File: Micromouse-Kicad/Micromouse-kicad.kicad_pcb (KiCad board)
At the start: 4 copper layers, 98.6 x 100 mm, 69 parts, among them J1 UARTBTH, J2 Batería, J3 VL6180x, J4 MotorEncodL, J5 MotorEncodR, Q1 BS170, Q2 BS170, Q3 BS170, Q4 BS170, SW1 PowerSwitch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

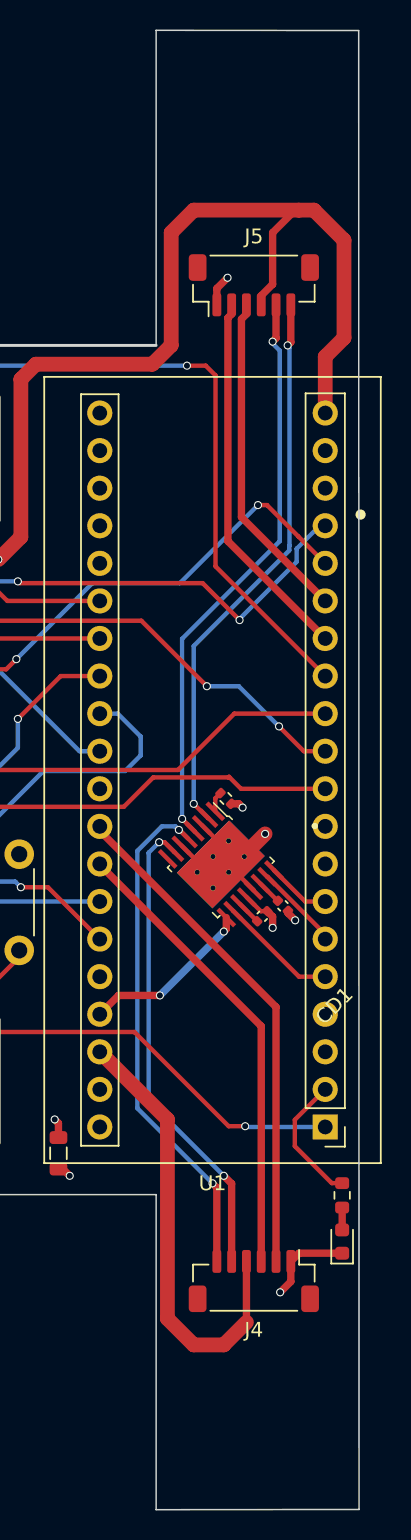
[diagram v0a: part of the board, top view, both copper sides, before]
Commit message: Modelos 3D completados
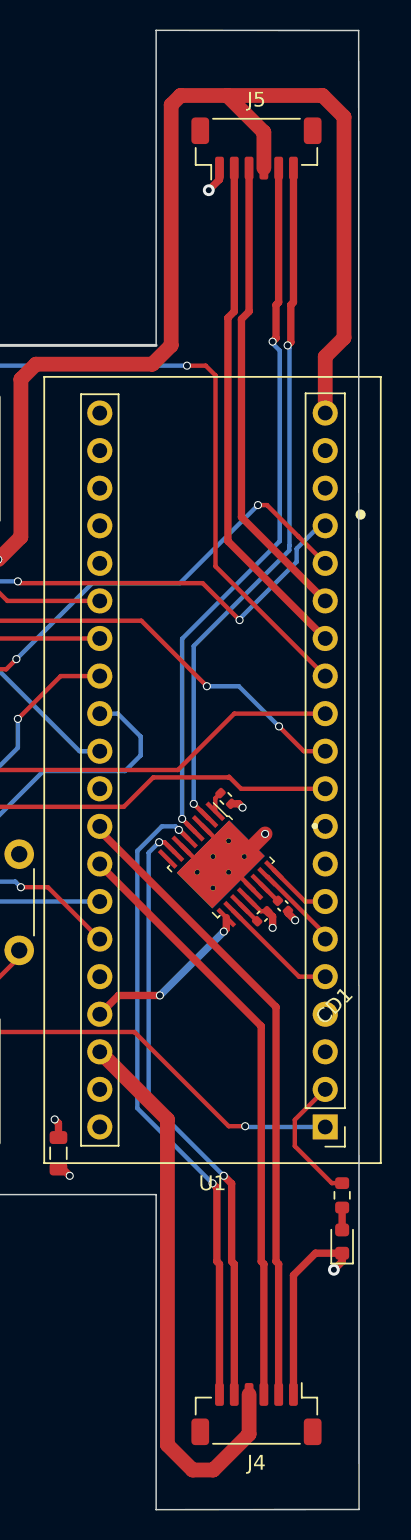
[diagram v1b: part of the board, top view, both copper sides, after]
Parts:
- moved J5 9.25 mm to (183.3, 60.6)
- moved J4 8.99 mm to (183.3, 146.2)
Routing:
- net +3.3V: track 144.7 -> 167.0 mm
- net TIM4_CH1: track 25.4 -> 34.7 mm
- net OutML2: track 39.0 -> 48.3 mm
- net OutML1: track 38.0 -> 47.3 mm
- net TIM4_CH2: track 22.5 -> 31.8 mm
- net TIM3_CH2: track 31.4 -> 40.5 mm
- net TIM3_CH1: track 34.3 -> 43.4 mm
- net OutMR2: track 34.4 -> 43.5 mm
- net OutMR1: track 32.3 -> 41.3 mm
- net GND: track 94.6 -> 101.5 mm

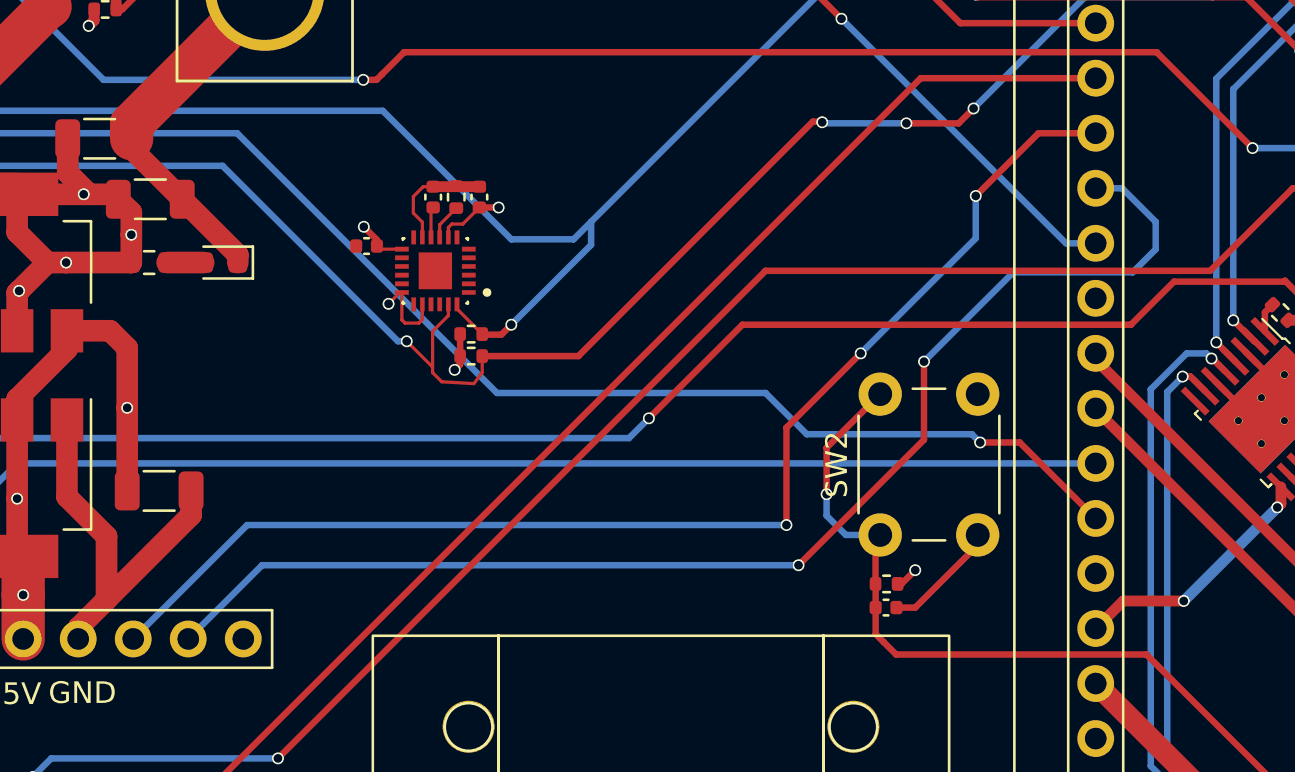
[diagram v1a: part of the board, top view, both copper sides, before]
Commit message: Arreglo bluetooth
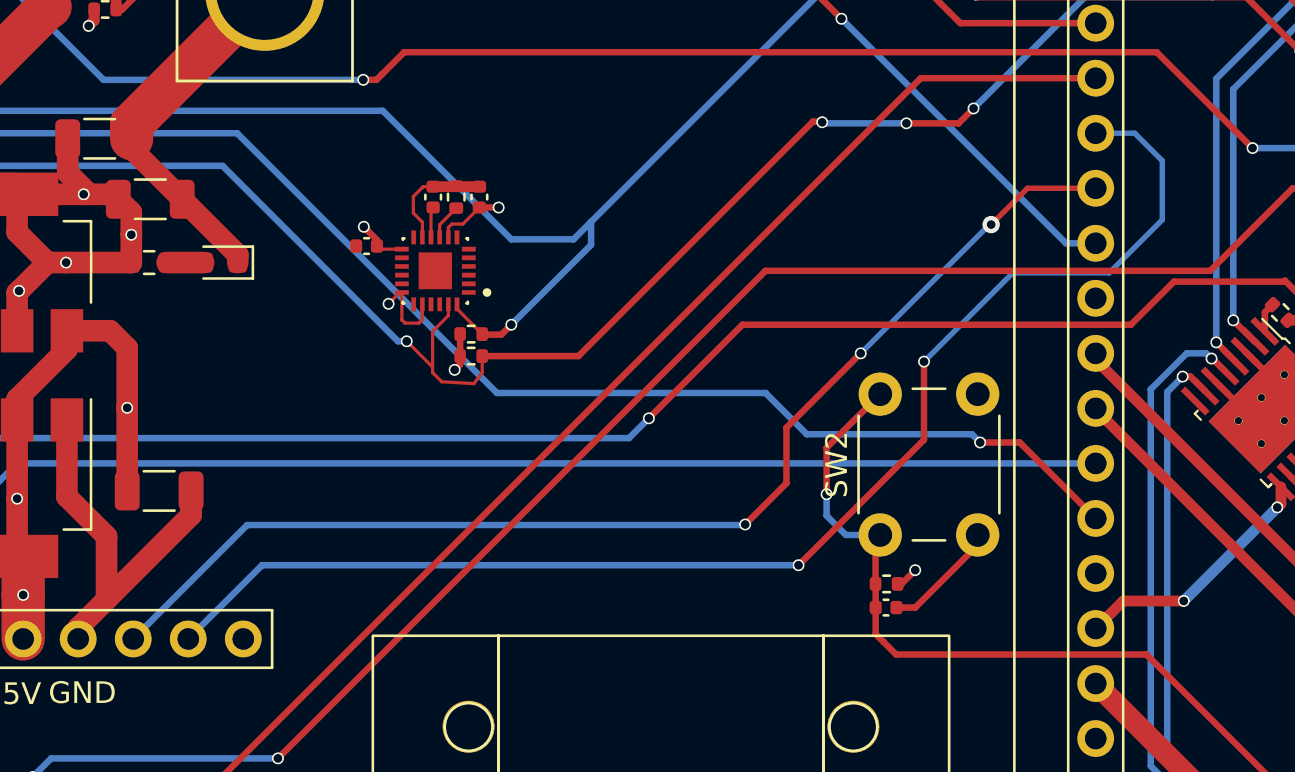
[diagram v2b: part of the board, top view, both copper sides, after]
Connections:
- U1 pad 28: UART4_RX -> UART4_TX
- U1 pad 29: UART4_TX -> UART4_RX
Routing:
- net UART4_RX: track 57.9 -> 54.5 mm
- net UART4_TX: track 58.9 -> 61.4 mm
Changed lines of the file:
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@@
       (rotate (xyz 0 0 0))
+    )
+    (model "C:/Users/Tatan/3D Objects/KicadModels/HC_05 Blue Tooth Module.stp"
+      (offset (xyz 5.5 -6.3 25.5))
+      (scale (xyz 1 1 1))
+      (rotate (xyz 90 180 -90))
     )
   )
@@
       (net 36 "R_Reciever") (pinfunction "PA1") (pintype "bidirectional"))
     (pad "28" thru_hole circle (at 15.24 30.48 180) (size 1.7 1.7) (drill 1) (layers *.Cu *.Mask)
-      (net 56 "UART4_RX") (pinfunction "PA2") (pintype "bidirectional"))
+      (net 57 "UART4_TX") (pinfunction "PA2") (pintype "bidirectional"))
     (pad "29" thru_hole circle (at 15.24 27.94 180) (size 1.7 1.7) (drill 1) (layers *.Cu *.Mask)
-      (net 57 "UART4_TX") (pinfunction "PA3") (pintype "bidirectional"))
+      (net 56 "UART4_RX") (pinfunction "PA3") (pintype "bidirectional"))
     (pad "30" thru_hole circle (at 15.24 25.4 180) (size 1.7 1.7) (drill 1) (layers *.Cu *.Mask)
       (net 44 "ADC_VBat") (pinfunction "PA4") (pintype "bidirectional"))
@@
   (segment (start 184.739447 111.460589) (end 183.569328 110.29047) (width 0.3) (layer "F.Cu") (net 54))
   (segment (start 184.760589 111.460589) (end 184.739447 111.460589) (width 0.3) (layer "F.Cu") (net 54))
-  (segment (start 170.0784 96.266) (end 172.72 96.266) (width 0.3) (layer "F.Cu") (net 56))
-  (segment (start 167.1828 99.1616) (end 170.0784 96.266) (width 0.3) (layer "F.Cu") (net 56))
+  (segment (start 158.4452 112.4204) (end 158.4452 109.855) (width 0.3) (layer "F.Cu") (net 56))
+  (segment (start 169.5704 98.806) (end 172.72 98.806) (width 0.25) (layer "F.Cu") (net 56))
+  (segment (start 156.5402 114.3254) (end 158.4452 112.4204) (width 0.3) (layer "F.Cu") (net 56))
   (segment (start 158.4452 109.855) (end 161.8742 106.426) (width 0.3) (layer "F.Cu") (net 56))
-  (segment (start 158.4452 114.3508) (end 158.4452 109.855) (width 0.3) (layer "F.Cu") (net 56))
-  (via (at 167.1828 99.1616) (size 0.55) (drill 0.4) (layers "F.Cu" "B.Cu") (net 56))
+  (segment (start 167.894 100.4824) (end 169.5704 98.806) (width 0.25) (layer "F.Cu") (net 56))
   (via (at 161.8742 106.426) (size 0.55) (drill 0.4) (layers "F.Cu" "B.Cu") (net 56))
-  (via (at 158.4452 114.3508) (size 0.55) (drill 0.4) (layers "F.Cu" "B.Cu") (net 56))
-  (segment (start 167.1828 101.1174) (end 167.1828 99.1616) (width 0.3) (layer "B.Cu") (net 56))
-  (segment (start 161.8742 106.426) (end 167.1828 101.1174) (width 0.3) (layer "B.Cu") (net 56))
-  (segment (start 133.5532 114.3508) (end 158.4452 114.3508) (width 0.3) (layer "B.Cu") (net 56))
-  (segment (start 128.295 119.609) (end 133.5532 114.3508) (width 0.3) (layer "B.Cu") (net 56))
+  (via (at 156.5402 114.3254) (size 0.55) (drill 0.4) (layers "F.Cu" "B.Cu") (net 56))
+  (via (at 167.894 100.4824) (size 0.8) (drill 0.4) (layers "F.Cu" "B.Cu") (net 56))
+  (segment (start 161.8742 106.426) (end 167.8178 100.4824) (width 0.25) (layer "B.Cu") (net 56))
+  (segment (start 156.5402 114.3254) (end 156.5148 114.3508) (width 0.3) (layer "B.Cu") (net 56))
+  (segment (start 167.8178 100.4824) (end 167.894 100.4824) (width 0.25) (layer "B.Cu") (net 56))
+  (segment (start 156.5148 114.3508) (end 133.5532 114.3508) (width 0.3) (layer "B.Cu") (net 56))
+  (segment (start 133.5532 114.3508) (end 128.295 119.609) (width 0.3) (layer "B.Cu") (net 56))
   (segment (start 164.7952 110.4138) (end 164.7952 106.807) (width 0.3) (layer "F.Cu") (net 57))
   (segment (start 159.004 116.205) (end 164.7952 110.4138) (width 0.3) (layer "F.Cu") (net 57))
   (via (at 159.004 116.205) (size 0.55) (drill 0.4) (layers "F.Cu" "B.Cu") (net 57))
   (via (at 164.7952 106.807) (size 0.55) (drill 0.4) (layers "F.Cu" "B.Cu") (net 57))
-  (segment (start 175.4886 100.3554) (end 173.9392 98.806) (width 0.3) (layer "B.Cu") (net 57))
   (segment (start 130.835 119.609) (end 134.239 116.205) (width 0.3) (layer "B.Cu") (net 57))
-  (segment (start 173.9392 98.806) (end 172.72 98.806) (width 0.3) (layer "B.Cu") (net 57))
-  (segment (start 168.9162 102.686) (end 174.428 102.686) (width 0.3) (layer "B.Cu") (net 57))
-  (segment (start 164.7952 106.807) (end 168.9162 102.686) (width 0.3) (layer "B.Cu") (net 57))
-  (segment (start 174.428 102.686) (end 175.4886 101.6254) (width 0.3) (layer "B.Cu") (net 57))
-  (segment (start 175.4886 101.6254) (end 175.4886 100.3554) (width 0.3) (layer "B.Cu") (net 57))
+  (segment (start 173.343558 102.711) (end 175.7934 100.261158) (width 0.25) (layer "B.Cu") (net 57))
+  (segment (start 174.5234 96.266) (end 172.72 96.266) (width 0.25) (layer "B.Cu") (net 57))
+  (segment (start 168.8912 102.711) (end 173.343558 102.711) (width 0.25) (layer "B.Cu") (net 57))
   (segment (start 134.239 116.205) (end 159.004 116.205) (width 0.3) (layer "B.Cu") (net 57))
+  (segment (start 175.7934 97.536) (end 174.5234 96.266) (width 0.25) (layer "B.Cu") (net 57))
+  (segment (start 164.7952 106.807) (end 168.8912 102.711) (width 0.25) (layer "B.Cu") (net 57))
+  (segment (start 175.7934 100.261158) (end 175.7934 97.536) (width 0.25) (layer "B.Cu") (net 57))
   (segment (start 183.8118 144.8266) (end 183.8118 136.0128) (width 0.5) (layer "F.Cu") (net 62))
   (segment (start 172.72 109.02) (end 172.72 108.966) (width 0.5) (layer "F.Cu") (net 62))
